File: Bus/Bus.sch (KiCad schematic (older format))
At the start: 31 parts, among them J1 Conn_01x22, J2 Conn_01x22, J3 Conn_01x22, J4 Conn_01x22, J5 Conn_01x16, J6 Conn_01x16, J7 Conn_01x16, J8 Conn_01x16, U1 74LS139, U2 SN74LS04N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

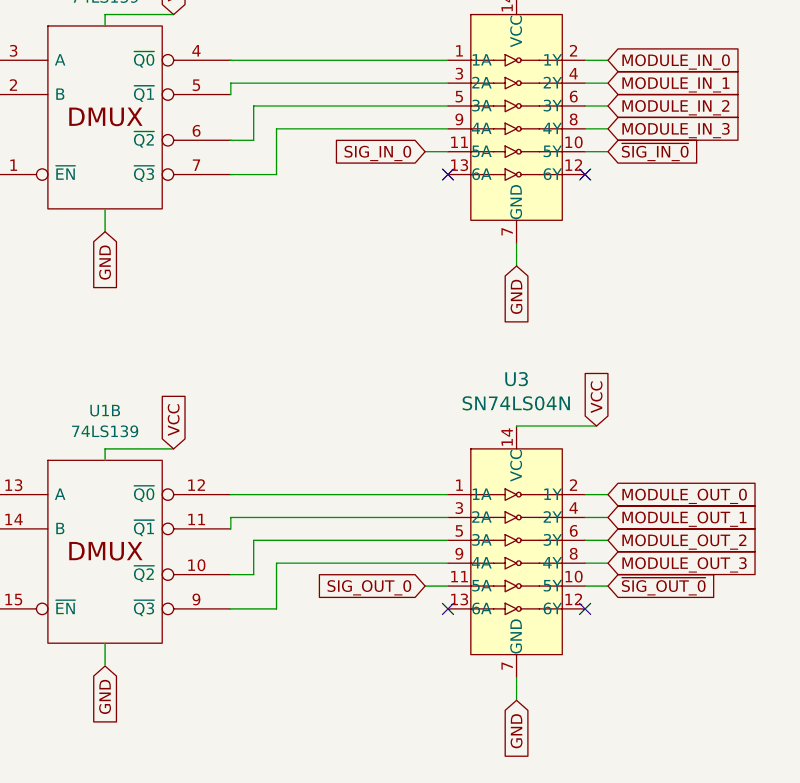
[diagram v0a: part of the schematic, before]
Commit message: Fixed floating inputs; improved power; added parts list; replaced JK latches
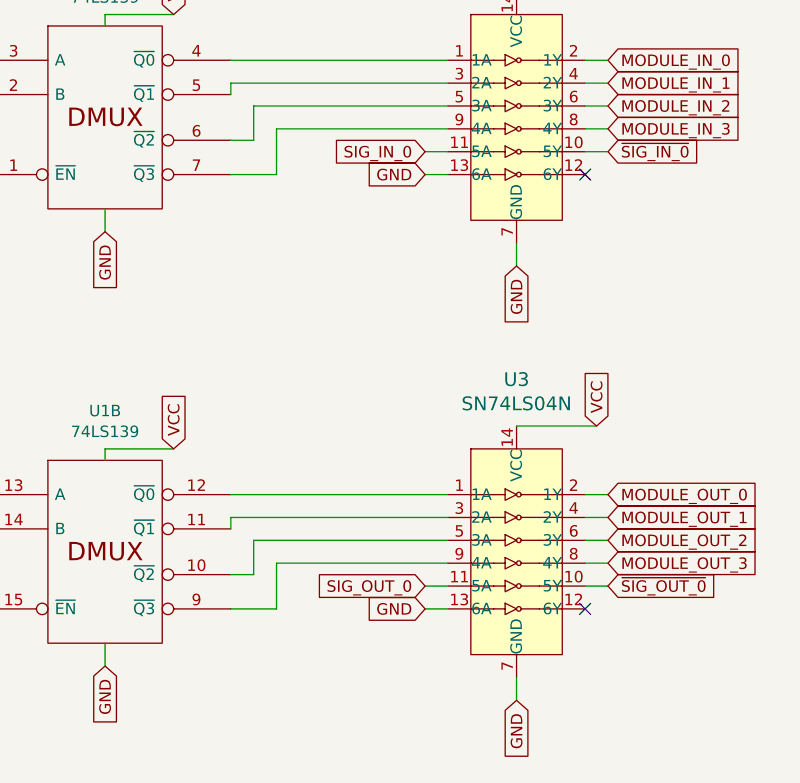
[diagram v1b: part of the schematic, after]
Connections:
- net GND: now also U2.13 (6A), U3.13 (6A)
- no-connect marks 4 -> 2
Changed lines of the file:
@@
 Module headers
 NoConn ~ 10450 2250
-NoConn ~ 9850 2250
 NoConn ~ 10450 4150
-NoConn ~ 9850 4150
 Wire Wire Line
 	1600 6150 1600 6300
@@
 Wire Wire Line
 	6450 5250 5500 5250
+Text GLabel 9750 2250 0    50   Input ~ 0
+GND
+Wire Wire Line
+	9750 2250 9850 2250
+Text GLabel 9750 4150 0    50   Input ~ 0
+GND
+Wire Wire Line
+	9750 4150 9850 4150
 $EndSCHEMATC
